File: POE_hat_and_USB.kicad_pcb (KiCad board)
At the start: 2 copper layers, 100 x 30 mm, 94 parts, among them J1 GPIO_CONNECTOR, J2 RJHSE-5385, J3 PIR Motion Sensor, J4 DH22T, J5 USB_A, J8 USB_B_Micro, Q1 DMG1012UW-7, U1 TPS54360B, U2 RTL8152B-VB, U3 FE1.1s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

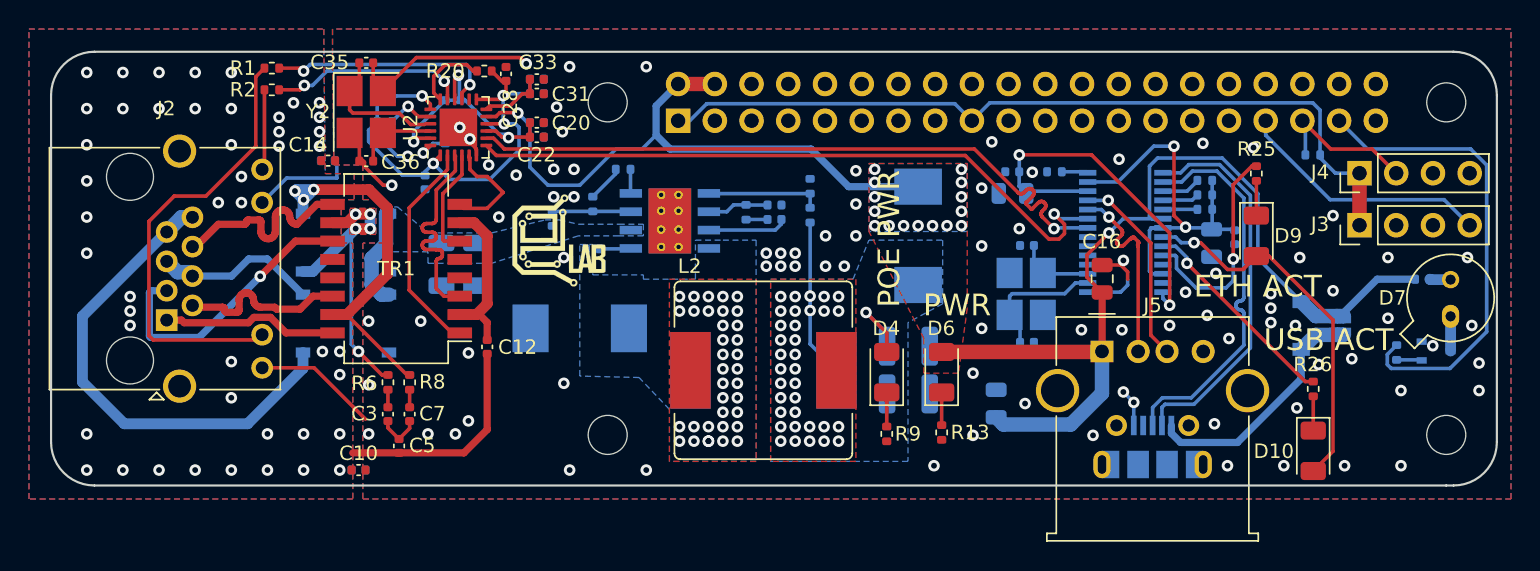
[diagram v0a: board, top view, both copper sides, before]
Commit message: Remove power supply and USB hub.
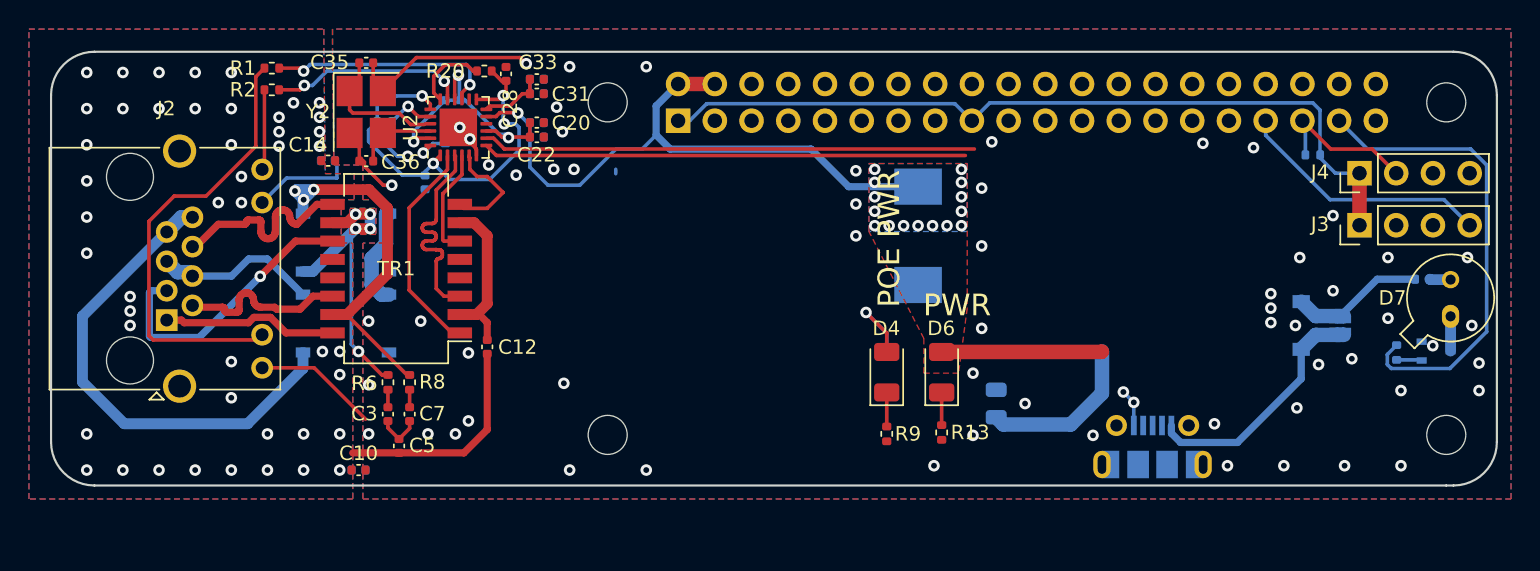
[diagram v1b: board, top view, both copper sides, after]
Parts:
- removed C1, C2: 2.2, Capacitor_SMD:C_1206_3216Metric
- removed C11, C13: 47, Capacitor_SMD:C_1210_3225Metric
- removed C16, C23, C38: 10, Capacitor_SMD:C_0805_2012Metric
- removed C25, C39, C4: 0.1, Capacitor_SMD:C_0402_1005Metric
- removed C32, C34: 10, Capacitor_SMD:C_0402_1005Metric
- removed C6: 750 pF, Capacitor_SMD:C_0402_1005Metric
- removed C8: 27, Capacitor_SMD:C_0402_1005Metric
- removed D10: L_USB1, LED_SMD:LED_1206_3216Metric
- removed D3: B560C, Diode_SMD:D_SMC
- removed D9: L_USB2, LED_SMD:LED_1206_3216Metric
- removed G***: LOGO, user-footprints:LOGO_eLAB_c=8,1mm
- removed J5: USB_A, Connector_USB:USB_A_Molex_67643_Horizontal
- removed L1, L2: 8.2 µH (SRR1210-8R2Y), Inductor_SMD:L_Bourns_SRR1210A
- removed R10: 75k, Resistor_SMD:R_0402_1005Metric
- removed R11: 12k, Resistor_SMD:R_0402_1005Metric
- removed R21, R22, R23: 100k, Resistor_SMD:R_0402_1005Metric
- removed R24, R25, R26: 2.7k, Resistor_SMD:R_0402_1005Metric
- removed R3: 520k, Resistor_SMD:R_0402_1005Metric
- removed R4: 80, Resistor_SMD:R_0402_1005Metric
- removed R5: 150k, Resistor_SMD:R_0402_1005Metric
- removed R7: 28.7k, Resistor_SMD:R_0402_1005Metric
- removed U1: TPS54360B, Package_SO:TI_SO-PowerPAD-8_ThermalVias
- removed U3: FE1.1s, Package_SO:SSOP-28_3.9x9.9mm_P0.635mm
- removed Y1: 12, Crystal:Crystal_SMD_3225-4Pin_3.2x2.5mm_HandSoldering
- D7: value LED_ALT -> OP293B
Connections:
- C24 pad 1: /VDD33 -> Net-(C24-Pad1)
- C26 pad 1: /VDD33 -> Net-(C24-Pad1)
- J8 pad 2: /USB_IN- -> /USB2-
- J8 pad 3: /USB_IN+ -> /USB2+
- U2 pad 10: /VDD33 -> Net-(C24-Pad1)
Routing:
- net +5V: track 110.6 -> 75.3 mm, vias 17 -> 16
- net +3V3: track 27.0 -> 0.00 mm, vias 2 -> 0
- net /USB_IN+: track 26.8 -> 0.00 mm
- net /USB_IN-: track 26.8 -> 0.00 mm
- net Net-(C23-Pad2): track 25.9 -> 0.00 mm, vias 2 -> 0
- net /DRV: track 25.9 -> 0.00 mm, vias 1 -> 0
- net /LED2: track 15.2 -> 0.00 mm, vias 1 -> 0
- net /LED1: track 14.5 -> 0.00 mm, vias 1 -> 0
- net /USB1-: track 13.6 -> 0.00 mm, vias 1 -> 0
- net GND: track 55.5 -> 41.9 mm, vias 87 -> 63
- net /USB1+: track 13.6 -> 0.00 mm, vias 1 -> 0
- net /USB2+: track 46.9 -> 33.4 mm, vias 1 -> 0
- net /USB2-: track 47.0 -> 34.1 mm, vias 1 -> 0
- net Net-(D4-Pad2): track 17.2 -> 6.26 mm, vias 35 -> 1
- net Net-(C34-Pad1): track 9.27 -> 0.00 mm
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- removed copper zone on B.Cu, net +VDC
- removed copper zone on B.Cu, net Net-(C4-Pad2)
- removed copper zone on F.Cu, net Net-(C4-Pad2)
- removed copper zone on B.Cu, net Net-(D4-Pad2)
- removed copper zone on F.Cu, net Net-(D4-Pad2)
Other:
- board text removed: "ETH ACT"
- board text removed: "USB ACT"

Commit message: Reroute PCB (removing USB hub, changing power supply and crystal).
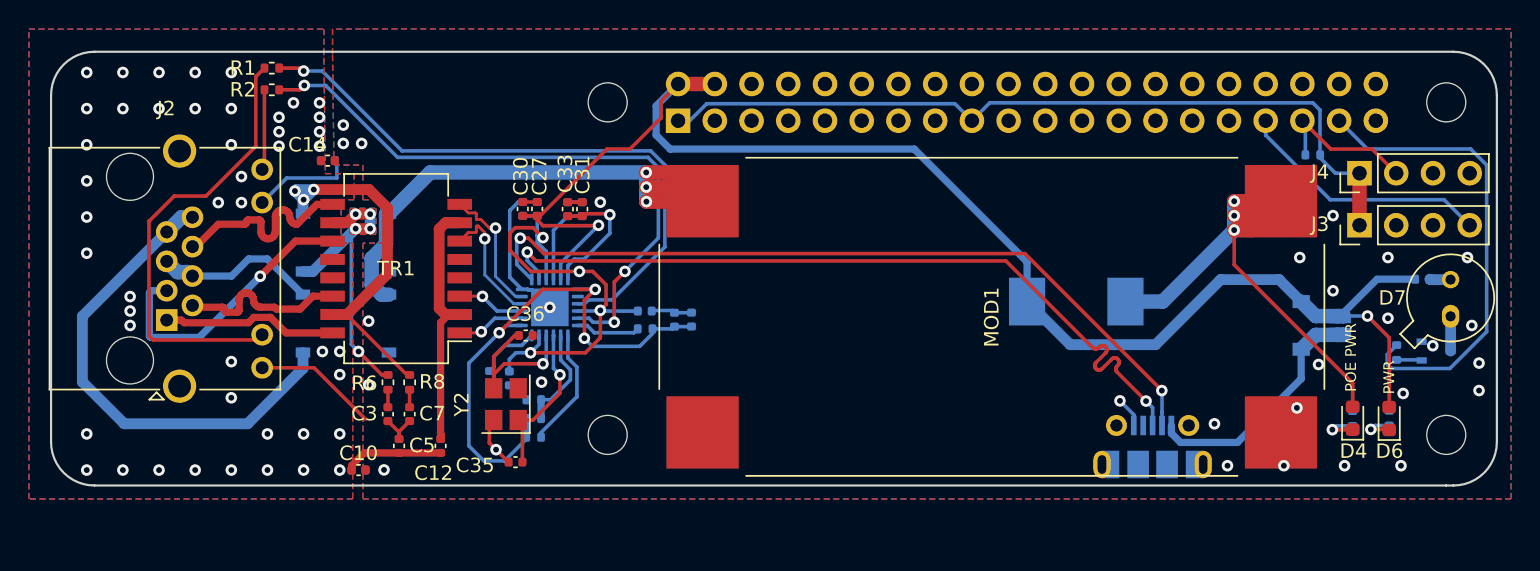
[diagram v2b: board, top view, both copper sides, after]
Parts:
- removed C37: 10, Capacitor_SMD:C_0805_2012Metric
- added MOD1: LM2596HVS, user-footprints:Module_LM2596HVS, F.Cu at (147.6, 109.4)
- C20, C22, C28, R13, R20, R9, U2: moved to B.Cu
- C27, C30: moved to F.Cu
- D4, D6: footprint LED_SMD:LED_1206_3216Metric -> LED_SMD:LED_0603_1608Metric
- Y2: value 25 MHz 30ppm -> 25 MHz 30ppm (HELE(Harmony Elec) X3S025000FC1H-HV); footprint Crystal:Crystal_SMD_3225-4Pin_3.2x2.5mm_HandSoldering -> Crystal:Crystal_SMD_3225-4Pin_3.2x2.5mm
- moved D4 32.4 mm to (172.6, 116.4)
- moved R9 32.2 mm to (172.6, 116.4), turned to 90 degrees
- moved D6 31.1 mm to (175.1, 116.4)
- moved R13 31.0 mm to (175.1, 116.4), turned to 90 degrees
- moved C35 29.5 mm to (114.7, 119.5), turned to 180 degrees
- moved R19 25.5 mm to (115.9, 117.7)
- moved R18 23.0 mm to (115.9, 116.4)
- moved Y2 22.4 mm to (114.0, 115.4), turned to 90 degrees
- moved C28 21.3 mm to (126.8, 109.6)
- moved R20 21.0 mm to (123.6, 110.2)
- moved R17 21.0 mm to (115.9, 115.1)
- moved C19 19.7 mm to (125.7, 109.6), turned to 90 degrees
- moved C21 19.3 mm to (114.2, 113.7)
- moved C29 19.0 mm to (123.6, 109.0), turned to 0 degrees
- moved R16 17.0 mm to (112.9, 113.7), turned to 90 degrees
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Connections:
- net Net-(D4-Pad2) renamed VDC
- U2 pad 7: /USB2+ -> /USB2-
- U2 pad 8: /USB2- -> /USB2+
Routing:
- net +VDC: track 7.00 -> 40.9 mm, vias 0 -> 3
- net VDC: track 6.26 -> 38.1 mm, vias 1 -> 3
- net /LED1_SPISCK: track 13.6 -> 43.3 mm, vias 2 -> 3
- net +5V: track 75.3 -> 104.3 mm, vias 16 -> 2
- net /LED0_SPICSB: track 16.0 -> 42.8 mm, vias 2 -> 1
- net /USB2+: track 33.4 -> 54.5 mm, vias 0 -> 2
- net /USB2-: track 34.1 -> 54.5 mm, vias 0 -> 2
- net /VDD10: track 18.3 -> 34.9 mm, vias 3 -> 4
- net /VDD33: track 26.2 -> 39.4 mm
- net /TD-: track 15.2 -> 4.72 mm, vias 0 -> 1
- net /TD+: track 15.1 -> 4.71 mm, vias 0 -> 1
- net Earth: track 15.2 -> 6.83 mm
- net GND: track 41.9 -> 35.9 mm, vias 63 -> 29
- net /XTAL2: track 5.56 -> 11.4 mm, vias 0 -> 1
- net Net-(C12-Pad1): track 12.5 -> 18.3 mm
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- removed copper zone on B.Cu, net +5V
- removed copper zone on F.Cu, net +5V
